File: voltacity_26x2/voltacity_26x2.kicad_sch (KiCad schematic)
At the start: 68 parts, among them J1 2-Pin JST, J2 2-Pin JST, J3 OLED_128x32, J4 78127-1128, SW1 Switch, SW3 EC11, SW4 EC11, SW5 EC11

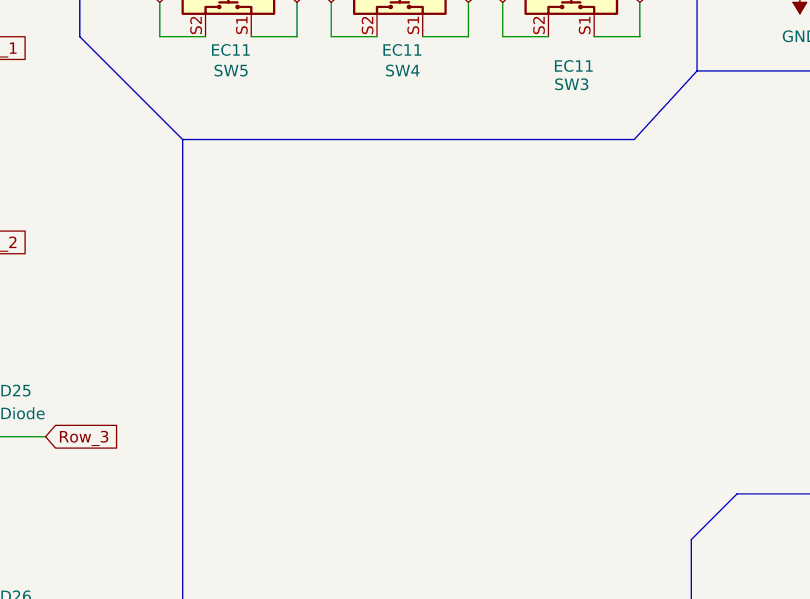
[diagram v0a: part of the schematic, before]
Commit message: Fixed the incorrect footprints for Kailh Choc hot-swap sockets
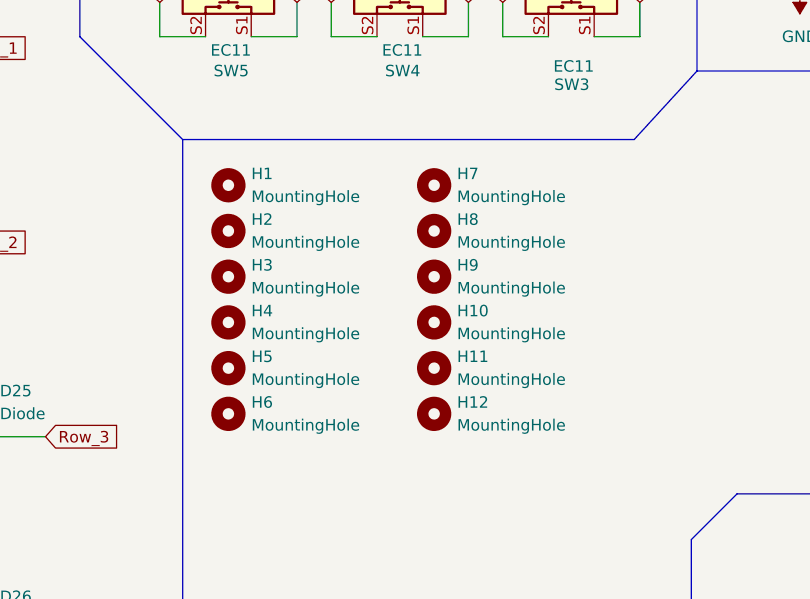
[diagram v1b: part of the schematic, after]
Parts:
- added H1, H10, H11, H12, H2, H3, H4, H5, H6, H7, H8, H9: MountingHole, MountingHole:MountingHole_2.2mm_M2_Pad_TopBottom, symbol Mechanical:MountingHole

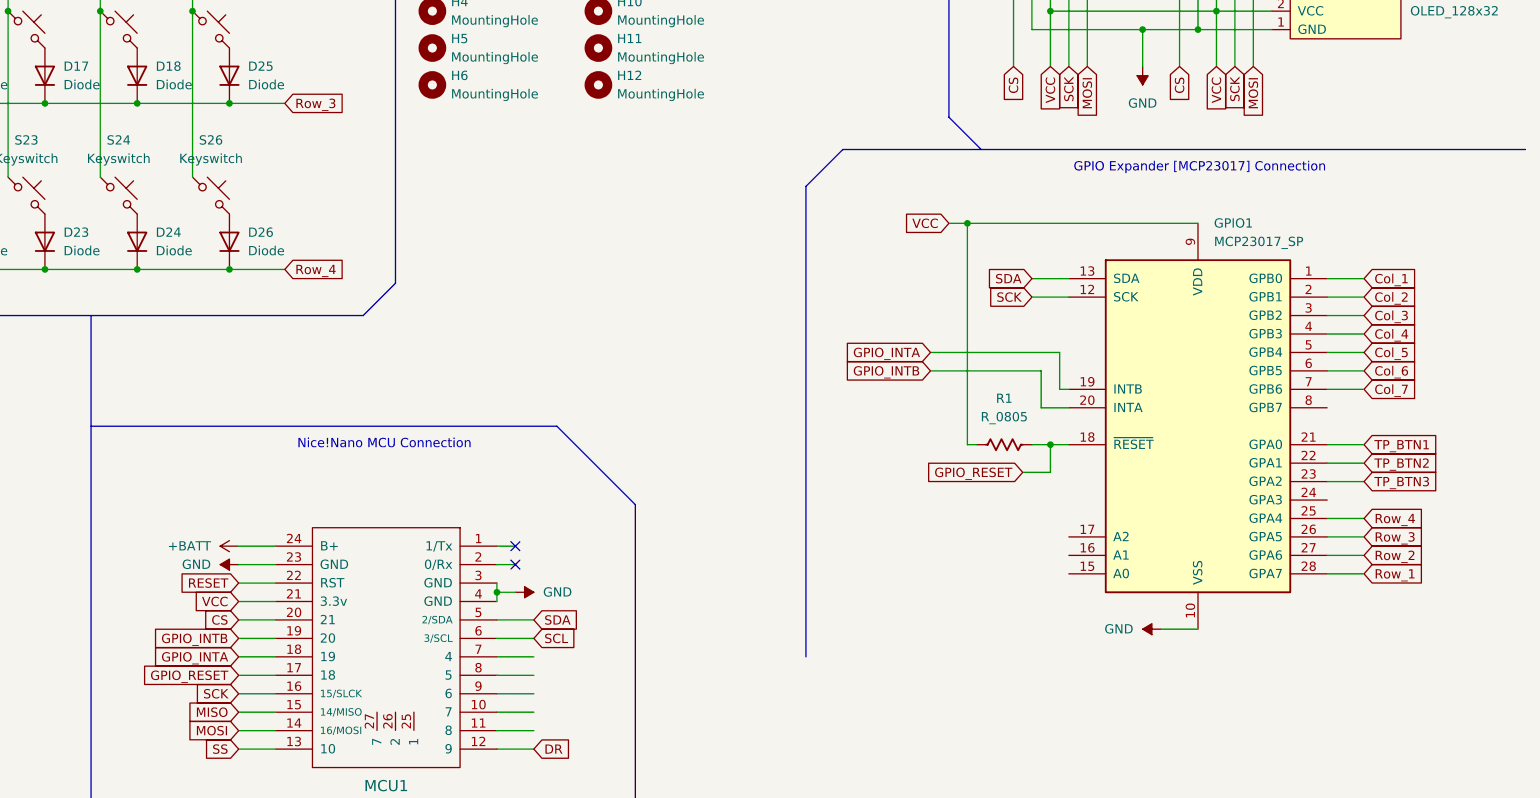
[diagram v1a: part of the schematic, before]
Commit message: Added new mounting holes
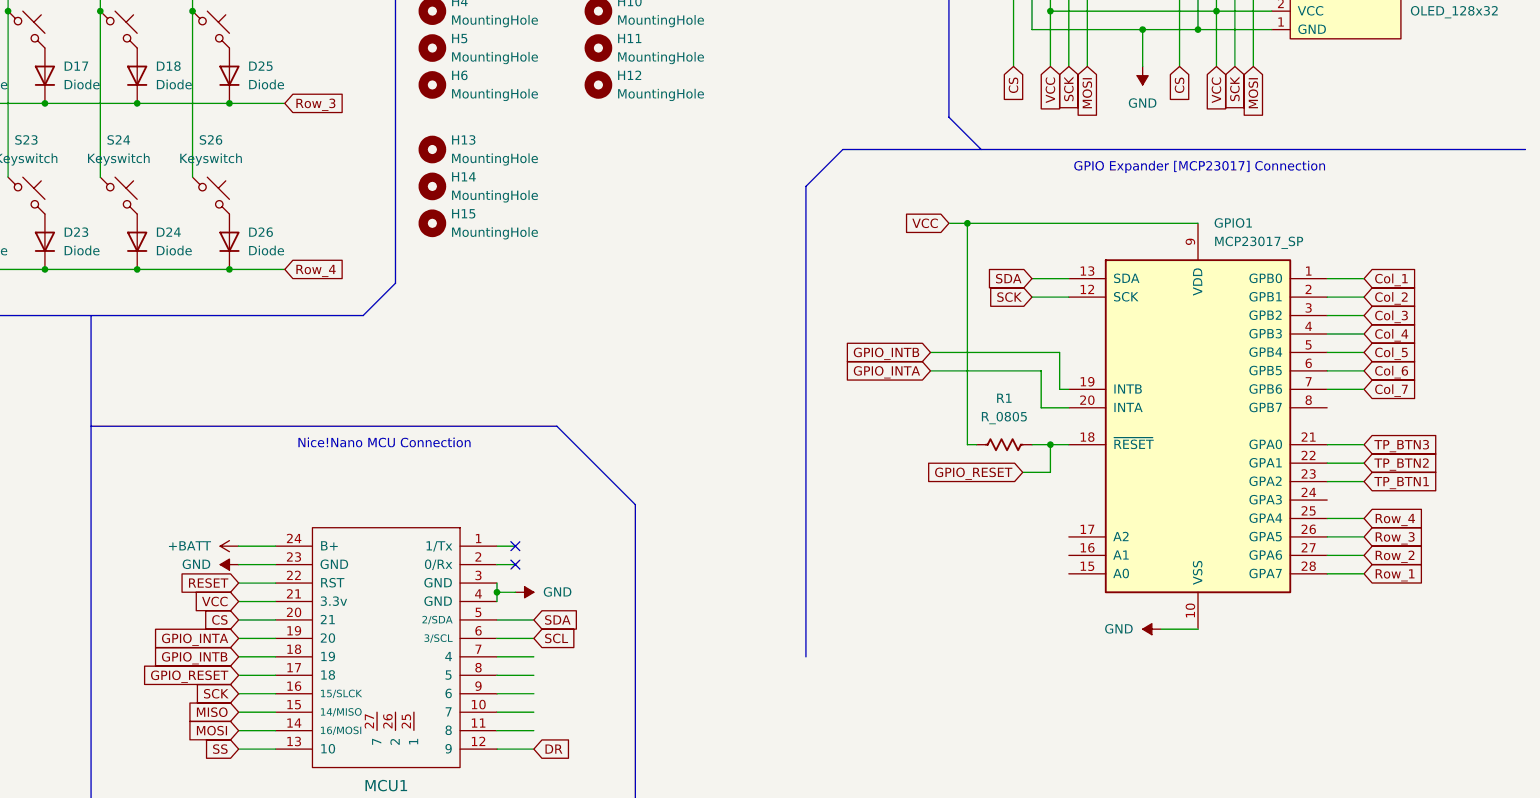
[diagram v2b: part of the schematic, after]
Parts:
- added H13, H14, H15: MountingHole, MountingHole:MountingHole_2.2mm_M2_Pad_TopBottom, symbol Mechanical:MountingHole
- S1, S10, S11, S12, S13, S14, S15, S16, S17, S18, S19, S2, S20, S21, S22, S23, S24, S25, S26, S3, S4, S5, S6, S7, S8, S9: footprint Kailh Sockets:REVERSED_Kailh_socket_PG1350_reversible -> marbastlib-choc:SW_choc_v1_HS_CPG135001S30_1u
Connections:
- net GPIO_INTA: now also GPIO1.20 (INTA), MCU1.19 (20); no longer GPIO1.19 (INTB), MCU1.18 (19)
- net GPIO_INTB: now also GPIO1.19 (INTB), MCU1.18 (19); no longer GPIO1.20 (INTA), MCU1.19 (20)
- net TP_BTN1: now also GPIO1.23 (GPA2); no longer GPIO1.21 (GPA0)
- net TP_BTN3: now also GPIO1.21 (GPA0); no longer GPIO1.23 (GPA2)

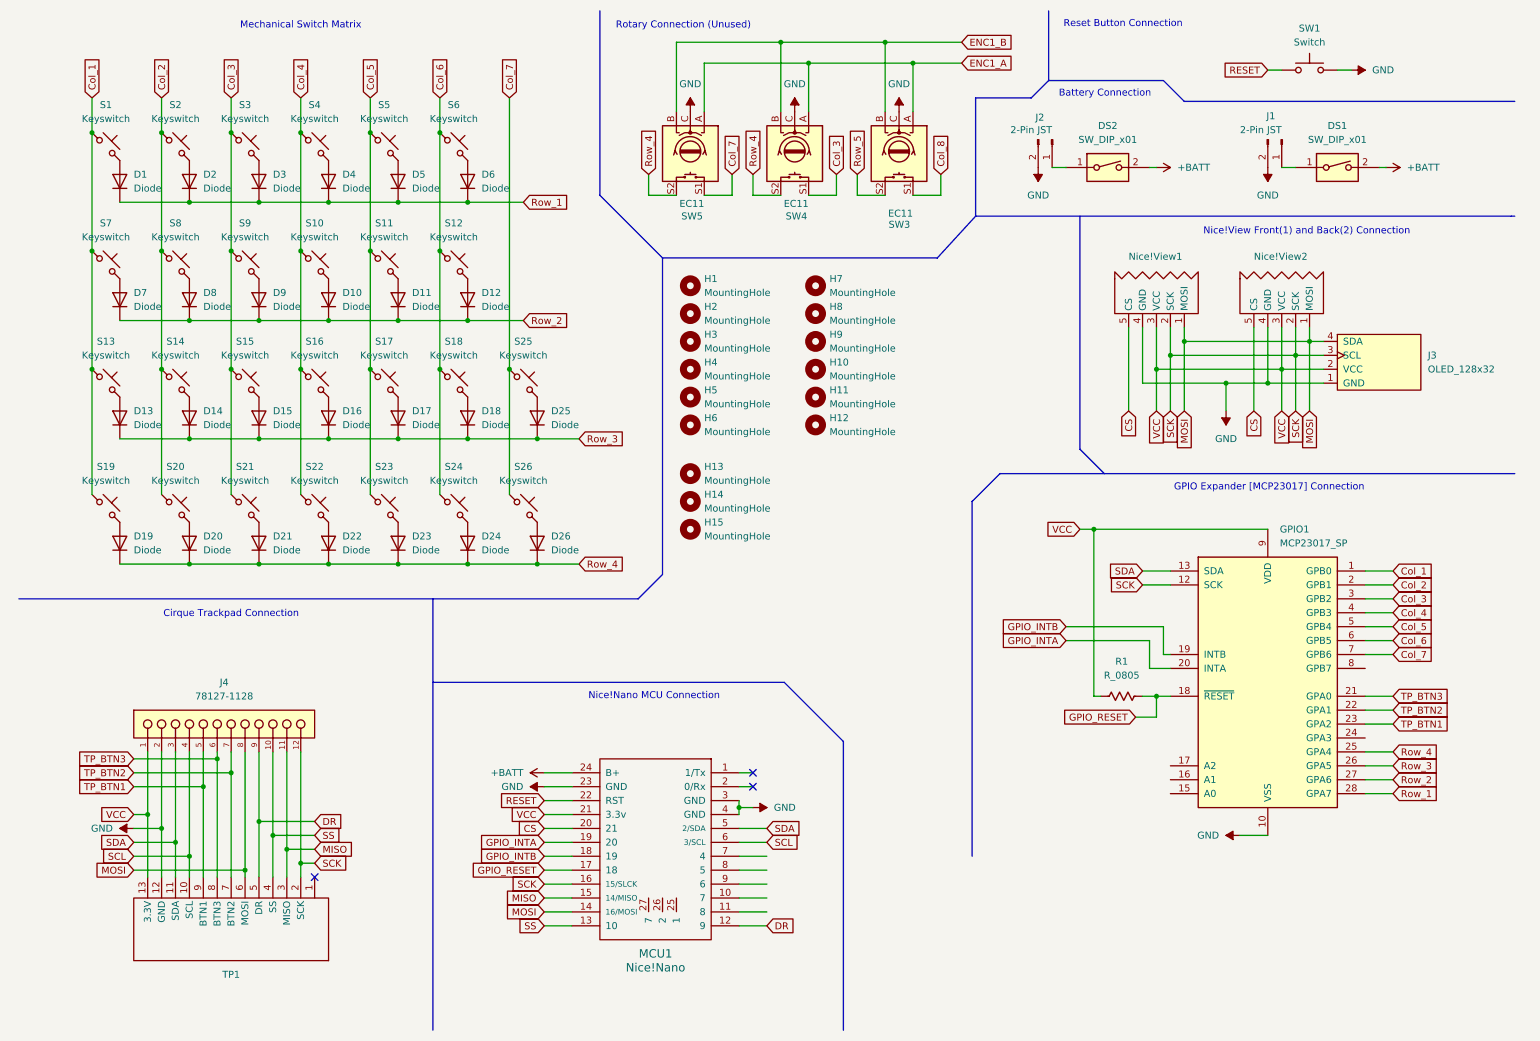
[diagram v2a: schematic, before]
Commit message: Updated schematic and cleaned up some options
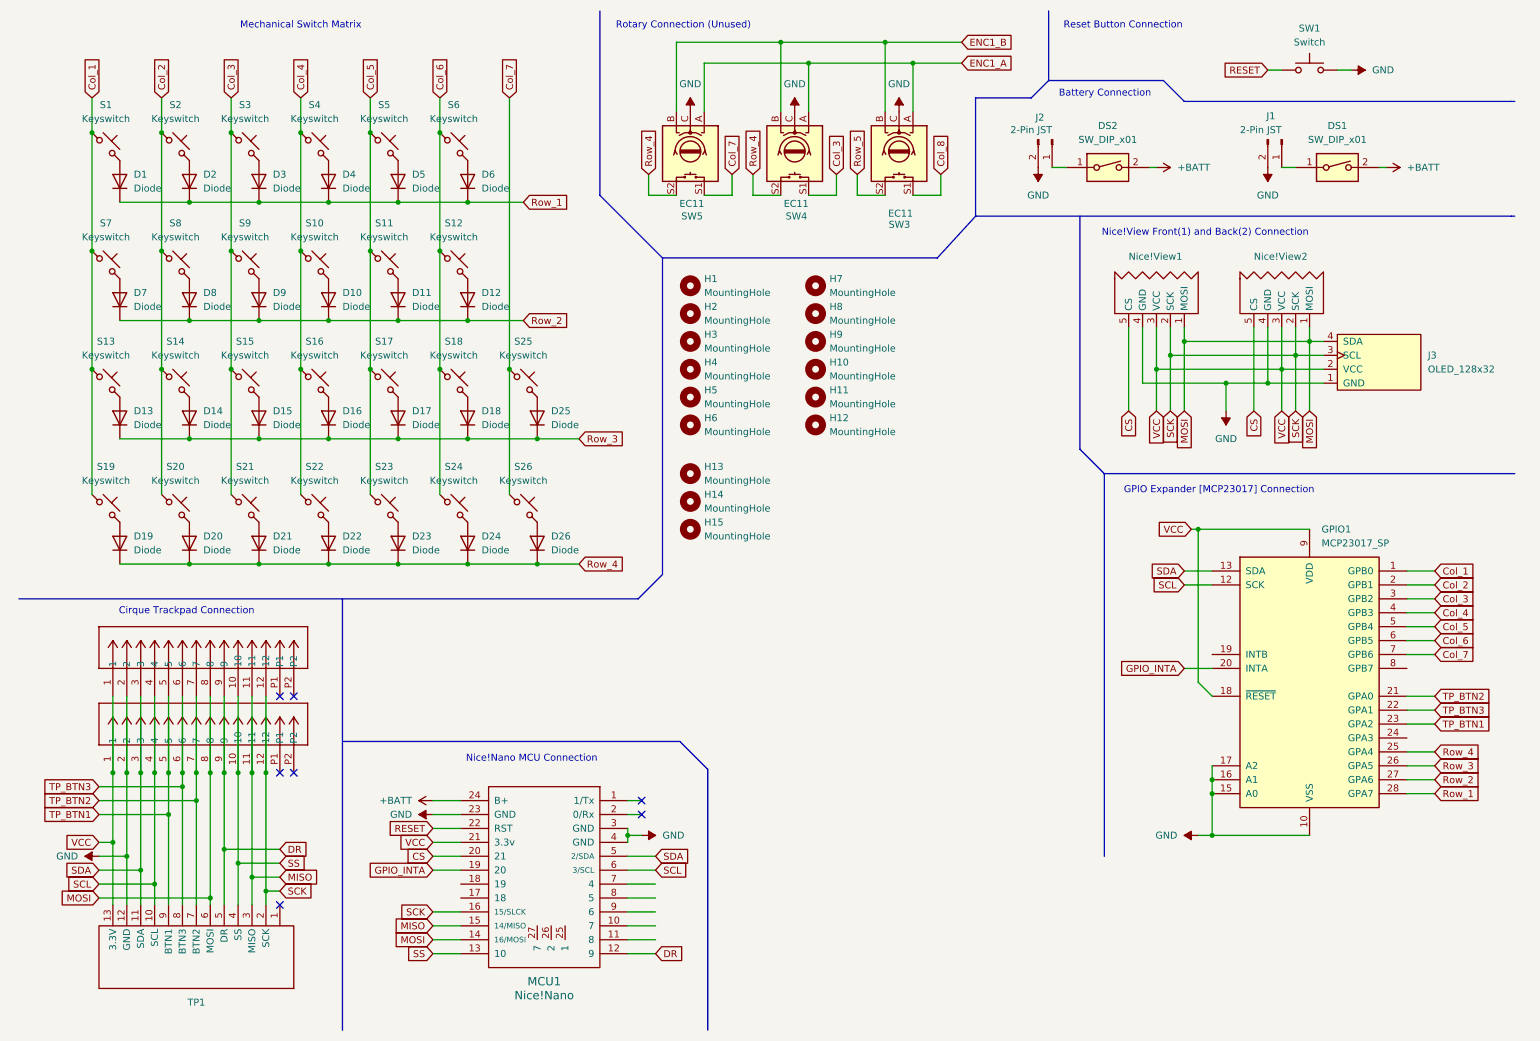
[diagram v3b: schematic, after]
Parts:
- removed R1: R_0805, PCM_Resistor_SMD_AKL:R_0805_2012Metric_Pad1.20x1.40mm_HandSolder, symbol PCM_Resistor_US_AKL:R_0805
- added J5: 78127-1128, CON_5051101297_MOL, symbol My_Keyboards_Library:5051101297
- J4: footprint Kicad Footprints:Molex-78127-1128-Manufacturer_Recommended -> CON_5051101297_MOL; symbol My_Keyboards_Library:78127-1128 -> My_Keyboards_Library:5051101297
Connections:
- net DR: now also J5.9
- net GND: now also GPIO1.15 (A0), GPIO1.16 (A1), GPIO1.17 (A2), J5.2
- net MISO: now also J5.11
- net MOSI: now also J5.8
- net SCK: now also J5.12; no longer GPIO1.12 (SCK)
- net SCL: now also GPIO1.12 (SCK), J5.4
- net SDA: now also J5.3
- net SS: now also J5.10
- net TP_BTN1: now also J5.5
- net TP_BTN2: now also GPIO1.21 (GPA0), J5.7; no longer GPIO1.22 (GPA1)
- net TP_BTN3: now also GPIO1.22 (GPA1), J5.6; no longer GPIO1.21 (GPA0)
- net VCC: now also GPIO1.18 (~{RESET}), J5.1
- net GPIO_INTB: no longer names the net of GPIO1.19 (INTB)
- net GPIO_INTB: no longer MCU1.18 (19)
- net GPIO_RESET: no longer names the net of MCU1.17 (18)
- net GPIO_RESET: no longer GPIO1.18 (~{RESET})
- no-connect marks 3 -> 7
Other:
- moved on the sheet: GPIO1, MCU1, TP1

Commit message: Added .blend of case & plate
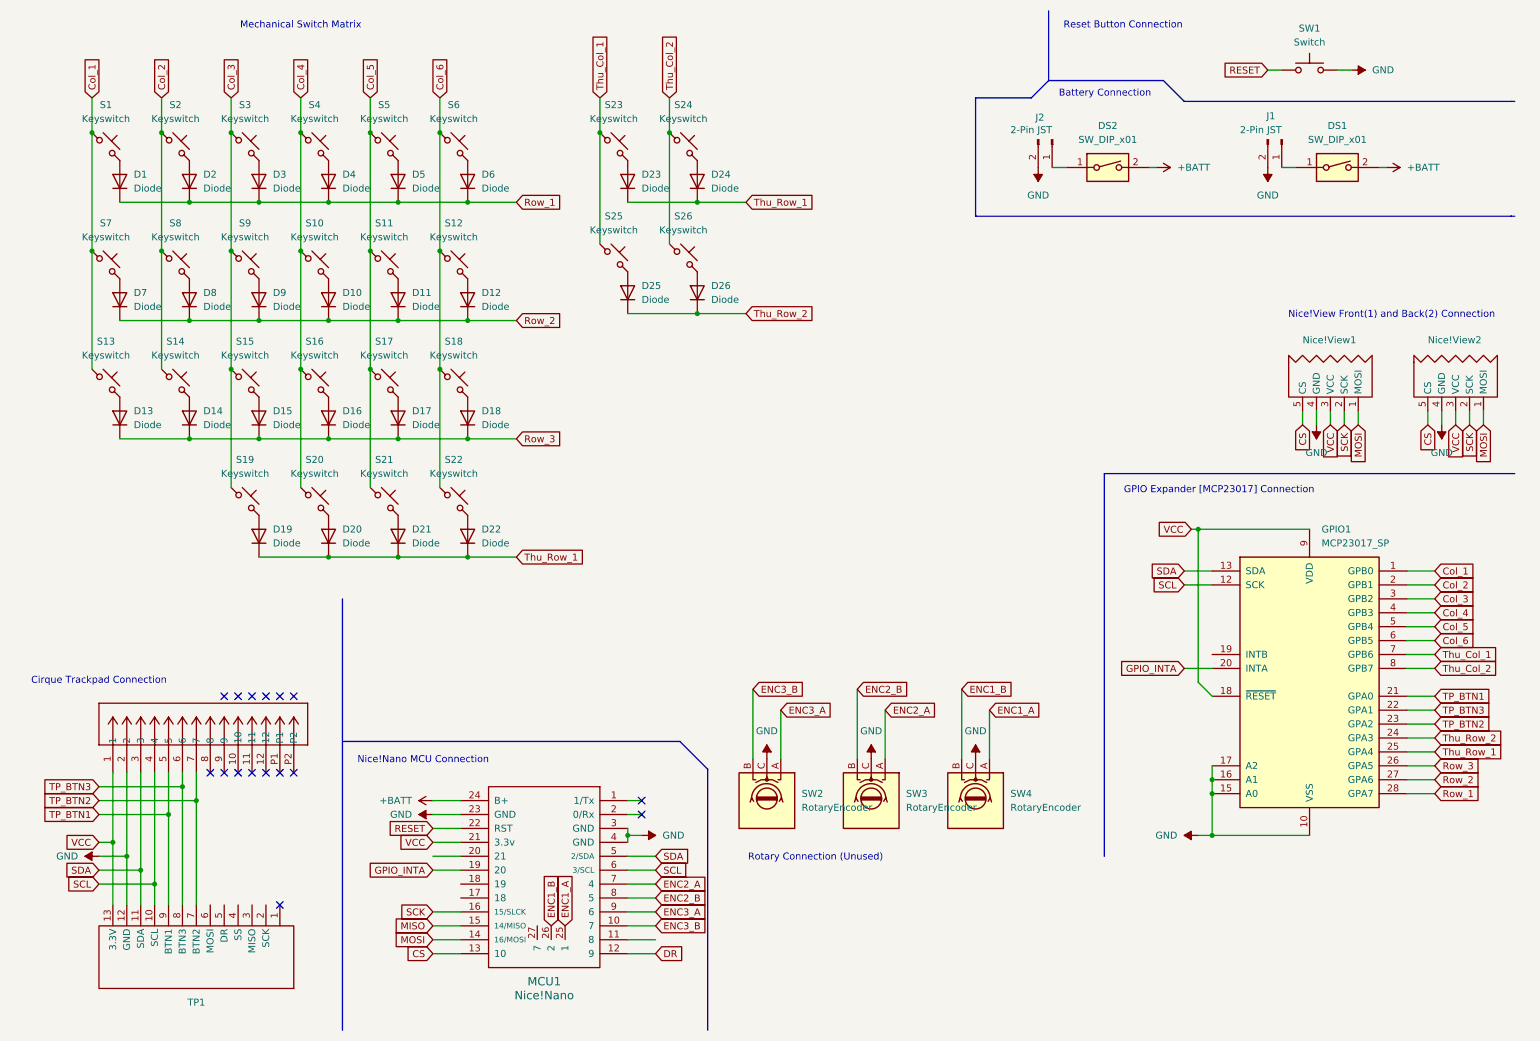
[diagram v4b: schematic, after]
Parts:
- removed H1, H10, H11, H12, H13, H14, H15, H2, H3, H4, H5, H6, H7, H8, H9: MountingHole, MountingHole:MountingHole_2.2mm_M2_Pad_TopBottom, symbol Mechanical:MountingHole
- removed J3: OLED_128x32, ScottoKeebs_Components:OLED_128x32, symbol ScottoKeebs:OLED_128x32
- removed J5: 78127-1128, CON_5051101297_MOL, symbol My_Keyboards_Library:5051101297
- removed SW3, SW4, SW5: EC11, Rotary_Encoder:RotaryEncoder_Alps_EC11E-Switch_Vertical_H20mm_CircularMountingHoles, symbol Device:RotaryEncoder_Switch
- added SW2, SW3, SW4: RotaryEncoder, Rotary_Encoder:RotaryEncoder_Alps_EC12E_Vertical_H20mm, symbol Device:RotaryEncoder
- J4: footprint CON_5051101297_MOL -> Kicad Footprints:CON_5051101297_MOL
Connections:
- net CS: now also MCU1.13 (10); no longer MCU1.20 (21)
- net Col_1: no longer S19.1
- net Col_2: no longer S20.1
- net Col_3: now also S19.1; no longer S21.1
- net Col_4: now also S20.1; no longer S22.1
- net Col_5: now also S21.1; no longer S23.1
- net Col_6: now also S22.1; no longer S24.1
- net DR: no longer J4.9, TP1.5 (DR)
- net ENC1_A: now also MCU1.25 (1), SW4.A
- net ENC1_B: now also MCU1.26 (2), SW4.B
- net GND: now also SW2.C, SW3.C, SW4.C
- net MISO: no longer J4.11, TP1.3 (MISO)
- net MOSI: no longer J4.8, TP1.6 (MOSI)
- net Row_3: no longer D25.1 (K)
- net SCK: no longer J4.12, TP1.2 (SCK)
- net TP_BTN1: now also GPIO1.21 (GPA0); no longer GPIO1.23 (GPA2)
- net TP_BTN2: now also GPIO1.23 (GPA2); no longer GPIO1.21 (GPA0)
- net Thu_Row_2: now reaches GPIO1.24 (GPA3)
- net Thu_Row_2: now also D25.1 (K), D26.1 (K)
- net Thu_Col_2: now reaches GPIO1.8 (GPB7)
- net Thu_Col_2: now also S24.1, S26.1
- net ENC3_B: now reaches MCU1.10 (7)
- net ENC3_B: now also SW2.B
- net ENC2_A: now reaches MCU1.7 (4)
- net ENC2_A: now also SW3.A
- net ENC2_B: now reaches MCU1.8 (5)
- net ENC2_B: now also SW3.B
- net ENC3_A: now reaches MCU1.9 (6)
- net ENC3_A: now also SW2.A
- net Col_7 renamed Thu_Col_1
- net Thu_Col_1: now also S23.1; no longer S26.1
- net Row_4 renamed Thu_Row_1
- net Thu_Row_1: no longer D26.1 (K)
- removed net SS: J4.10, MCU1.13 (10), TP1.4 (SS)
- no-connect marks 7 -> 16
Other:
- moved on the sheet: D19, D20, D21, D22, D24, D26, Nice!View1, Nice!View2, S19, S20, S21, S22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
